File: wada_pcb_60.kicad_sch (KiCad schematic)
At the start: 62 parts, among them J1 USB_C_Receptacle_USB2.0_16P, J2 USB_A, J3 USB_A, U1 XC6206PxxxMR, U2 STM32F072C8T6, U3 MIC2026-2BN, U4 FE1.1, U5 SRV05-4, U6 SRV05-4, U7 SRV05-4, Y1 12MHz

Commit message: wired up the LEDS, rows, and columns!
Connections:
- net D_USB1+: now also J3.3 (D+), U7.3 (IO2); no longer J2.3 (D+), U6.3 (IO2)
- net D_USB1-: now also J3.2 (D-), U7.4 (IO3); no longer J2.2 (D-), U6.4 (IO3)
- net D_USB2+: now also J2.3 (D+), U6.3 (IO2); no longer J3.3 (D+), U7.3 (IO2)
- net D_USB2-: now also J2.2 (D-), U6.4 (IO3); no longer J3.2 (D-), U7.4 (IO3)
- net PORT1_PWR: now also C26.1, C27.1, C28.1, J3.1 (VBUS), U7.5 (VP); no longer C23.1, C24.1, C25.1, J2.1 (VBUS), U6.5 (VP)
- net PORT2_PWR: now also C23.1, C24.1, C25.1, J2.1 (VBUS), U6.5 (VP); no longer C26.1, C27.1, C28.1, J3.1 (VBUS), U7.5 (VP)
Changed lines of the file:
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@@
 	(wire
 		(pts
-			(xy 478.79 72.39) (xy 472.44 72.39)
+			(xy 477.52 72.39) (xy 472.44 72.39)
 		)
 		(stroke
@@
 	(wire
 		(pts
-			(xy 87.63 180.34) (xy 76.2 180.34)
+			(xy 25.4 180.34) (xy 13.97 180.34)
 		)
 		(stroke
@@
 	(wire
 		(pts
-			(xy 39.37 207.01) (xy 50.8 207.01)
+			(xy 101.6 207.01) (xy 113.03 207.01)
 		)
 		(stroke
@@
 	(wire
 		(pts
-			(xy 101.6 207.01) (xy 113.03 207.01)
+			(xy 39.37 207.01) (xy 50.8 207.01)
 		)
 		(stroke
@@
 	(wire
 		(pts
-			(xy 25.4 180.34) (xy 15.24 180.34)
+			(xy 87.63 180.34) (xy 77.47 180.34)
 		)
 		(stroke
@@
 	(wire
 		(pts
-			(xy 114.3 129.54) (xy 102.87 129.54)
+			(xy 71.12 129.54) (xy 59.69 129.54)
 		)
 		(stroke
@@
 	(wire
 		(pts
-			(xy 483.87 67.31) (xy 472.44 67.31)
+			(xy 472.44 67.31) (xy 480.06 67.31)
 		)
 		(stroke
@@
 	(wire
 		(pts
-			(xy 483.87 69.85) (xy 472.44 69.85)
+			(xy 472.44 69.85) (xy 480.06 69.85)
 		)
 		(stroke
@@
 	(wire
 		(pts
-			(xy 71.12 129.54) (xy 60.96 129.54)
+			(xy 114.3 129.54) (xy 104.14 129.54)
 		)
 		(stroke
@@
 		)
 	)
-	(text "for USB-A no.2"
+	(text "for USB-A no.1"
 		(exclude_from_sim no)
 		(at 99.06 120.65 0)
@@
 		)
 	)
-	(text "for USB-A no.1"
+	(text "for USB-A no.2"
 		(exclude_from_sim no)
 		(at 55.88 120.65 0)
@@
 	)
 	(label "PORT2_PWR"
-		(at 113.03 207.01 180)
+		(at 50.8 207.01 180)
 		(effects
 			(font
@@
 	)
 	(label "PORT1_PWR"
-		(at 60.96 129.54 0)
+		(at 104.14 129.54 0)
 		(effects
 			(font
@@
 	)
 	(label "PORT1_PWR"
-		(at 50.8 207.01 180)
+		(at 113.03 207.01 180)
 		(effects
 			(font
@@
 	)
 	(label "PORT1_PWR"
-		(at 15.24 180.34 0)
+		(at 77.47 180.34 0)
 		(effects
 			(font
@@
 	)
 	(label "PORT2_PWR"
-		(at 102.87 129.54 0)
+		(at 59.69 129.54 0)
 		(effects
 			(font
@@
 	)
 	(label "PORT2_PWR"
-		(at 76.2 180.34 0)
+		(at 13.97 180.34 0)
 		(effects
 			(font
@@
 	(global_label "D_STM32+"
 		(shape bidirectional)
-		(at 483.87 69.85 0)
+		(at 480.06 69.85 0)
 		(fields_autoplaced yes)
 		(effects
@@
 		)
 		(property "Intersheetrefs" "${INTERSHEET_REFS}"
-			(at 497.824 69.85 0)
+			(at 494.014 69.85 0)
 			(effects
 				(font
@@
 	(global_label "D_USB1-"
 		(shape bidirectional)
-		(at 40.64 214.63 0)
+		(at 102.87 214.63 0)
 		(fields_autoplaced yes)
 		(effects
@@
 		)
 		(property "Intersheetrefs" "${INTERSHEET_REFS}"
-			(at 53.566 214.63 0)
+			(at 115.796 214.63 0)
 			(effects
 				(font
@@
 	(global_label "D_USB2-"
 		(shape bidirectional)
-		(at 128.27 148.59 0)
+		(at 85.09 148.59 0)
 		(fields_autoplaced yes)
 		(effects
@@
 		)
 		(property "Intersheetrefs" "${INTERSHEET_REFS}"
-			(at 141.196 148.59 0)
+			(at 98.016 148.59 0)
 			(effects
 				(font
@@
 	(global_label "D_USB2+"
 		(shape bidirectional)
-		(at 128.27 143.51 0)
+		(at 85.09 143.51 0)
 		(fields_autoplaced yes)
 		(effects
@@
 		)
 		(property "Intersheetrefs" "${INTERSHEET_REFS}"
-			(at 141.196 143.51 0)
+			(at 98.016 143.51 0)
 			(effects
 				(font
@@
 	(global_label "RGB_LED"
 		(shape input)
-		(at 478.79 72.39 0)
+		(at 477.52 72.39 0)
 		(fields_autoplaced yes)
 		(effects
@@
 		)
 		(property "Intersheetrefs" "${INTERSHEET_REFS}"
-			(at 489.9999 72.39 0)
+			(at 488.7299 72.39 0)
 			(effects
 				(font
@@
 	(global_label "D_USB2+"
 		(shape bidirectional)
-		(at 102.87 212.09 0)
+		(at 40.64 212.09 0)
 		(fields_autoplaced yes)
 		(effects
@@
 		)
 		(property "Intersheetrefs" "${INTERSHEET_REFS}"
-			(at 115.796 212.09 0)
+			(at 53.566 212.09 0)
 			(effects
 				(font
@@
 	(global_label "D_STM32-"
 		(shape bidirectional)
-		(at 483.87 67.31 0)
+		(at 480.06 67.31 0)
 		(fields_autoplaced yes)
 		(effects
@@
 		)
 		(property "Intersheetrefs" "${INTERSHEET_REFS}"
-			(at 497.824 67.31 0)
+			(at 494.014 67.31 0)
 			(effects
 				(font
@@
 	(global_label "D_USB1-"
 		(shape bidirectional)
-		(at 85.09 148.59 0)
+		(at 128.27 148.59 0)
 		(fields_autoplaced yes)
 		(effects
@@
 		)
 		(property "Intersheetrefs" "${INTERSHEET_REFS}"
-			(at 98.016 148.59 0)
+			(at 141.196 148.59 0)
 			(effects
 				(font
@@
 	(global_label "D_USB1+"
 		(shape bidirectional)
-		(at 85.09 143.51 0)
+		(at 128.27 143.51 0)
 		(fields_autoplaced yes)
 		(effects
@@
 		)
 		(property "Intersheetrefs" "${INTERSHEET_REFS}"
-			(at 98.016 143.51 0)
+			(at 141.196 143.51 0)
 			(effects
 				(font
@@
 	(global_label "D_USB2-"
 		(shape bidirectional)
-		(at 102.87 214.63 0)
+		(at 40.64 214.63 0)
 		(fields_autoplaced yes)
 		(effects
@@
 		)
 		(property "Intersheetrefs" "${INTERSHEET_REFS}"
-			(at 115.796 214.63 0)
+			(at 53.566 214.63 0)
 			(effects
 				(font
@@
 	(global_label "D_USB1+"
 		(shape bidirectional)
-		(at 40.64 212.09 0)
+		(at 102.87 212.09 0)
 		(fields_autoplaced yes)
 		(effects
@@
 		)
 		(property "Intersheetrefs" "${INTERSHEET_REFS}"
-			(at 53.566 212.09 0)
+			(at 115.796 212.09 0)
 			(effects
 				(font

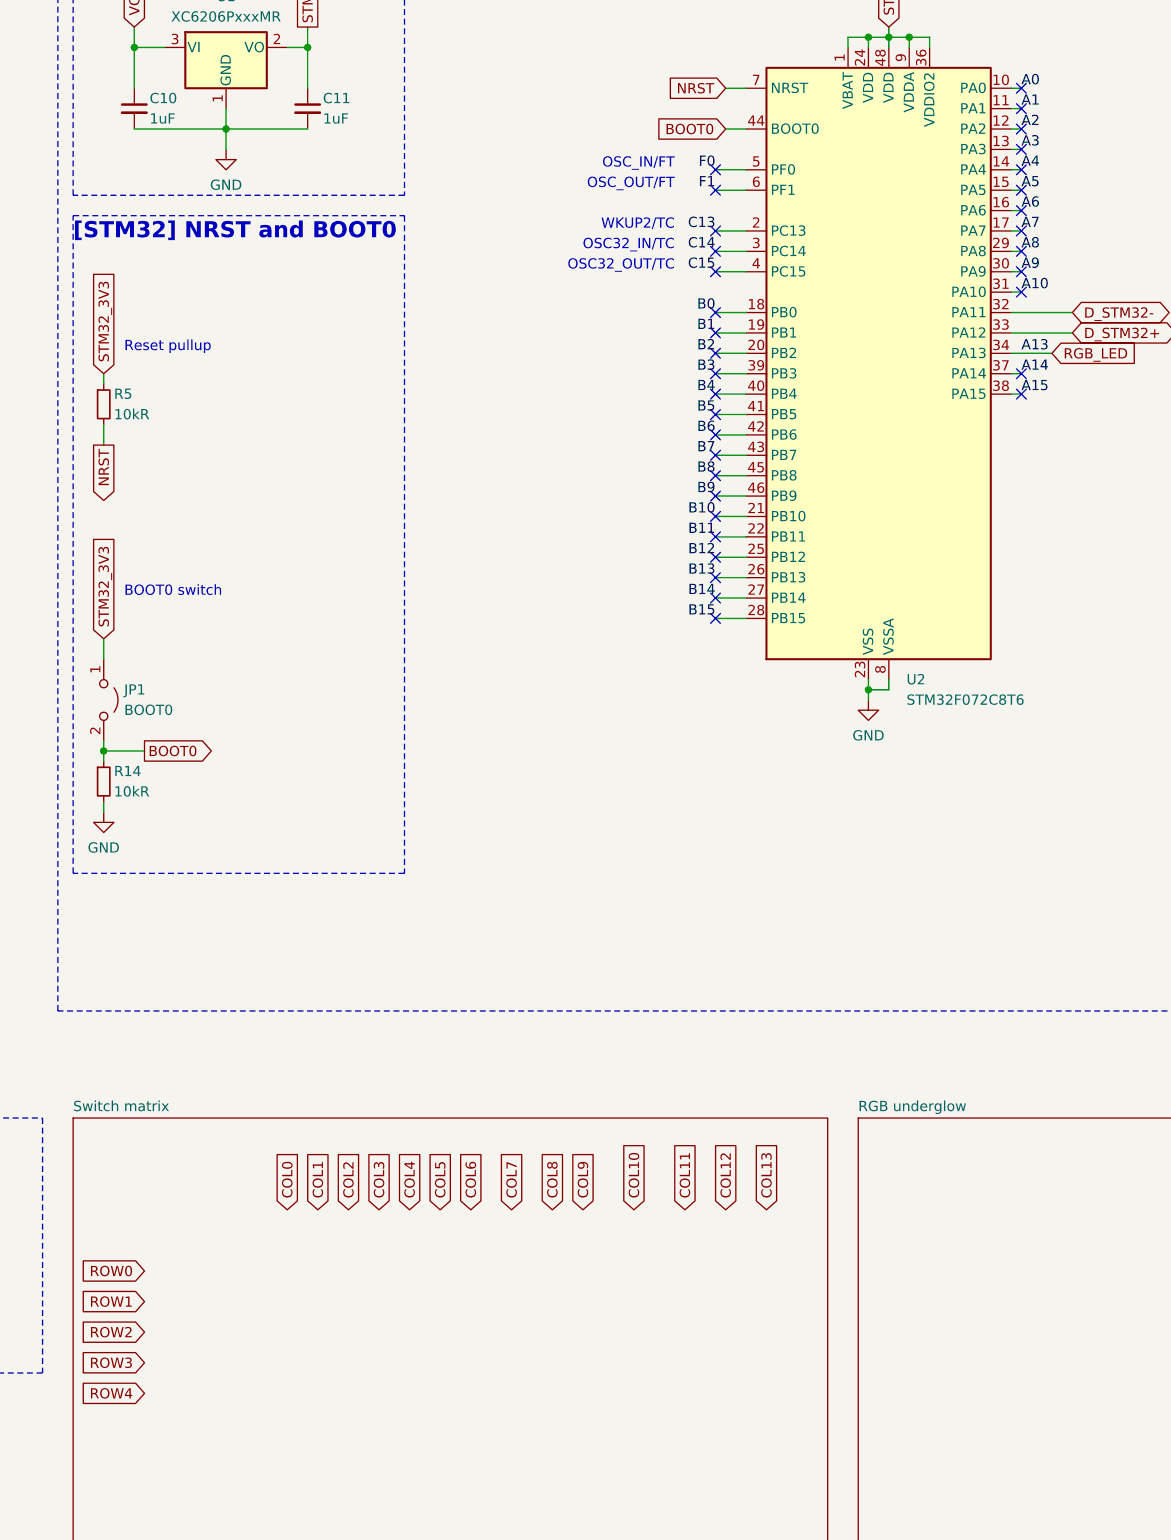
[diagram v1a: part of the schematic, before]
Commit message: done! missing the reset switch!
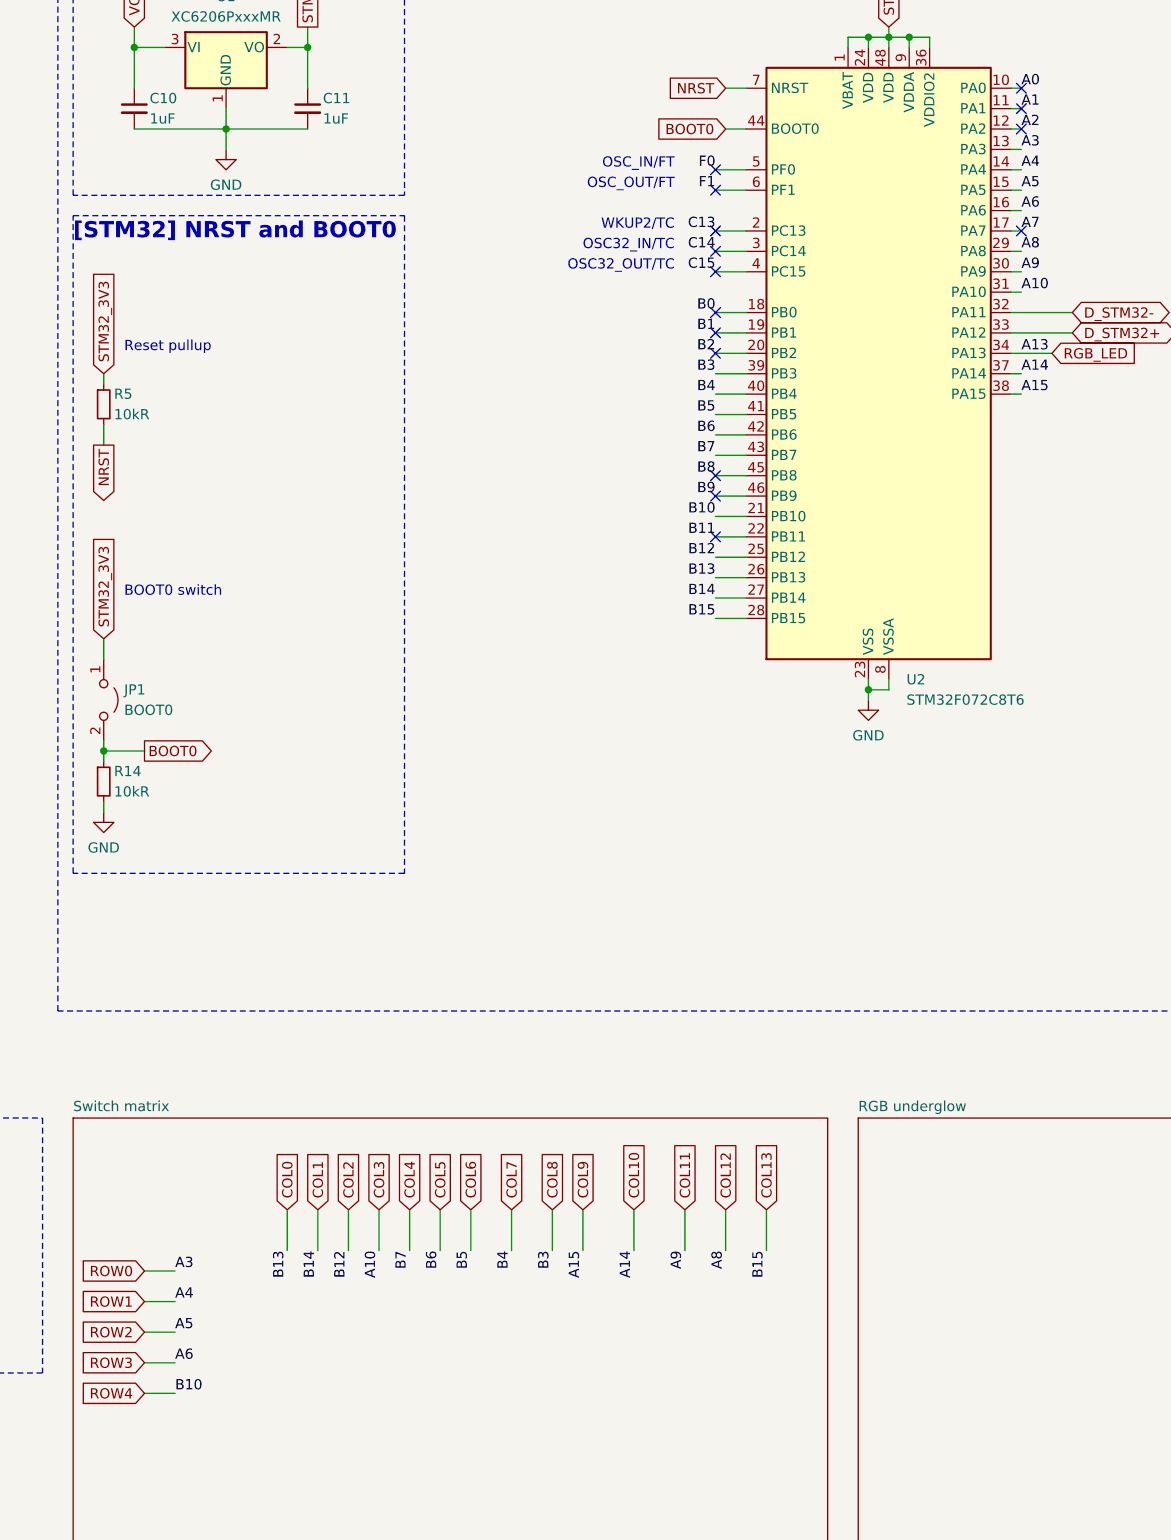
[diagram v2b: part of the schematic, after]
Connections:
- net A10 is gone; now on net COL3: U2.31 (PA10)
- net A14 is gone; now on net COL10: U2.37 (PA14)
- net A15 is gone; now on net COL9: U2.38 (PA15)
- net A3 is gone; now on net ROW0: U2.13 (PA3)
- net A4 is gone; now on net ROW1: U2.14 (PA4)
- net A5 is gone; now on net ROW2: U2.15 (PA5)
- net A6 is gone; now on net ROW3: U2.16 (PA6)
- net A8 is gone; now on net COL12: U2.29 (PA8)
- net A9 is gone; now on net COL11: U2.30 (PA9)
- net B10 is gone; now on net ROW4: U2.21 (PB10)
- net B12 is gone; now on net COL2: U2.25 (PB12)
- net B13 is gone; now on net COL0: U2.26 (PB13)
- net B14 is gone; now on net COL1: U2.27 (PB14)
- net B15 is gone; now on net COL13: U2.28 (PB15)
- net B3 is gone; now on net COL8: U2.39 (PB3)
- net B4 is gone; now on net COL7: U2.40 (PB4)
- net B5 is gone; now on net COL6: U2.41 (PB5)
- net B6 is gone; now on net COL5: U2.42 (PB6)
- net B7 is gone; now on net COL4: U2.43 (PB7)
- no-connect marks 48 -> 29

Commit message: review time!
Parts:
- removed JP1: BOOT0, Connector_PinHeader_2.54mm:PinHeader_1x02_P2.54mm_Vertical, symbol Jumper:Jumper_2_Open
- removed R5: 10kR, Resistor_SMD:R_0603_1608Metric, symbol Device:R_Small
- added BOOT_SW1, RESET_SW1: SW_SPST, Button_Switch_SMD:SW_SPST_TL3342, symbol Switch:SW_SPST
- added C47: 100nF, Capacitor_SMD:C_0603_1608Metric, symbol Device:C_Small
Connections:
- net BOOT0: now also BOOT_SW1.2 (B)
- net GND: now also C47.1, RESET_SW1.2 (B)
- net NRST: now also C47.2, RESET_SW1.1 (A)
- net STM32_3V3: now also BOOT_SW1.1 (A)
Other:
- note removed: "Reset pullup"

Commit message: Changed USB type-A and LED parts
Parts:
- J2, J3: footprint cipulot_parts:USB-SMT-04F-S1-B1-R9A -> JING_USB-A:JING 903-231A2031S10100
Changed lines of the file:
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@@
 			)
 		)
-		(property "Footprint" "cipulot_parts:USB-SMT-04F-S1-B1-R9A"
+		(property "Footprint" "JING_USB-A:JING 903-231A2031S10100"
 			(at 97.79 213.36 0)
 			(effects
@@
 			)
 		)
-		(property "Footprint" "cipulot_parts:USB-SMT-04F-S1-B1-R9A"
+		(property "Footprint" "JING_USB-A:JING 903-231A2031S10100"
 			(at 35.56 213.36 0)
 			(effects
